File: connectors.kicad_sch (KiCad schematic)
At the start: 67 parts

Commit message: Cosmetic changes
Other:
- moved on the sheet: C?, D?, FB?, J?, Q?, R?, S?, TP?, U?

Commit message: Updated schematic
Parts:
- added J?: JST_XH_1x2_S2B-XH-A-LF-SN, antmicro-footprints:Conn_JST_XH_1x2_S2B-XH-A-LF-SN, symbol antmicroWire2BoardConnectors:JST_XH_1x2_S2B-XH-A-LF-SN
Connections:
- net GND: now also J?.1
- net PSU_ON: now also J?.2
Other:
- note added: "front panel switch connector"
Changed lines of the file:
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@@
   (junction (at 140.97 201.93) (diameter 0) (color 0 0 0 0)
   )
+  (junction (at 190.5 74.295) (diameter 0) (color 0 0 0 0)
+  )
   (junction (at 181.61 210.185) (diameter 0) (color 0 0 0 0)
   )
@@
   (junction (at 140.97 209.55) (diameter 0) (color 0 0 0 0)
   )
+  (junction (at 205.74 77.47) (diameter 0) (color 0 0 0 0)
+  )
   (no_connect (at 203.2 60.325))
   (no_connect (at 116.84 49.53))
@@
     (stroke (width 0) (type default) (color 0 0 0 0))
   )
+  (wire (pts (xy 195.58 83.185) (xy 190.5 83.185))
+    (stroke (width 0) (type default) (color 0 0 0 0))
+  )
   (wire (pts (xy 325.755 85.09) (xy 328.295 85.09))
     (stroke (width 0) (type default) (color 0 0 0 0))
@@
     (stroke (width 0) (type default) (color 0 0 0 0))
   )
+  (wire (pts (xy 198.12 83.185) (xy 198.12 77.47))
+    (stroke (width 0) (type default) (color 0 0 0 0))
+  )
   (wire (pts (xy 64.135 184.15) (xy 65.405 184.15))
     (stroke (width 0) (type default) (color 0 0 0 0))
@@
     (stroke (width 0) (type default) (color 0 0 0 0))
   )
+  (wire (pts (xy 190.5 74.295) (xy 190.5 83.185))
+    (stroke (width 0) (type default) (color 0 0 0 0))
+  )
   (wire (pts (xy 80.01 64.77) (xy 82.55 64.77))
     (stroke (width 0) (type default) (color 0 0 0 0))
@@
     (stroke (width 0) (type default) (color 0 0 0 0))
   )
+  (wire (pts (xy 205.74 77.47) (xy 205.74 78.105))
+    (stroke (width 0) (type default) (color 0 0 0 0))
+  )
   (wire (pts (xy 104.14 156.845) (xy 104.14 159.385))
     (stroke (width 0) (type default) (color 0 0 0 0))
@@
     (stroke (width 0) (type default) (color 0 0 0 0))
   )
+  (wire (pts (xy 198.12 77.47) (xy 205.74 77.47))
+    (stroke (width 0) (type default) (color 0 0 0 0))
+  )
   (wire (pts (xy 104.14 203.2) (xy 104.14 205.74))
     (stroke (width 0) (type default) (color 0 0 0 0))
@@
     (stroke (width 0) (type default) (color 0 0 0 0))
   )
-  (wire (pts (xy 205.74 74.295) (xy 205.74 78.105))
+  (wire (pts (xy 205.74 74.295) (xy 205.74 77.47))
     (stroke (width 0) (type default) (color 0 0 0 0))
   )
@@
     (effects (font (size 2.9972 2.9972)) (justify left bottom))
   )
+  (text "front panel switch connector" (at 186.055 92.075 0)
+    (effects (font (size 1.27 1.27)) (justify left bottom))
+  )
   (text "Power Indicators" (at 327.66 179.705 0)
     (effects (font (size 2.9972 2.9972)) (justify left bottom))
@@
     )
     (pin "1")
+    (pin "2")
+  )
+  (symbol (lib_id "antmicroWire2BoardConnectors:JST_XH_1x2_S2B-XH-A-LF-SN") (at 198.12 83.185 270) (unit 1)
+    (in_bom yes) (on_board yes) (fields_autoplaced)
+    (property "Reference" "J?" (id 0) (at 200.152 86.1644 90)
+      (effects (font (size 1.27 1.27) (thickness 0.15)) (justify left))
+    )
+    (property "Value" "JST_XH_1x2_S2B-XH-A-LF-SN" (id 1) (at 187.96 108.585 0)
+      (effects (font (size 1.27 1.27) (thickness 0.15)) (justify left bottom) hide)
+    )
+    (property "Footprint" "antmicro-footprints:Conn_JST_XH_1x2_S2B-XH-A-LF-SN" (id 2) (at 185.42 108.585 0)
+      (effects (font (size 1.27 1.27) (thickness 0.15)) (justify left bottom) hide)
+    )
+    (property "Datasheet" "https://www.tme.eu/Document/0a99312bb6c67d3f0f7869fe9a023cea/XH.pdf" (id 3) (at 182.88 108.585 0)
+      (effects (font (size 1.27 1.27) (thickness 0.15)) (justify left bottom) hide)
+    )
+    (property "MPN" "S2B-XH-A(LF)(SN)" (id 4) (at 200.152 88.6881 90)
+      (effects (font (size 1.27 1.27) (thickness 0.15)) (justify left))
+    )
+    (property "Manufacturer" "JST Automotive Connectors" (id 5) (at 190.5 108.585 0)
+      (effects (font (size 1.27 1.27) (thickness 0.15)) (justify left bottom) hide)
+    )
+    (property "Author" "Antmicro" (id 6) (at 180.34 108.585 0)
+      (effects (font (size 1.27 1.27) (thickness 0.15)) (justify left bottom) hide)
+    )
+    (property "License" "Apache-2.0" (id 7) (at 177.8 108.585 0)
+      (effects (font (size 1.27 1.27) (thickness 0.15)) (justify left bottom) hide)
+    )
+    (pin "1")

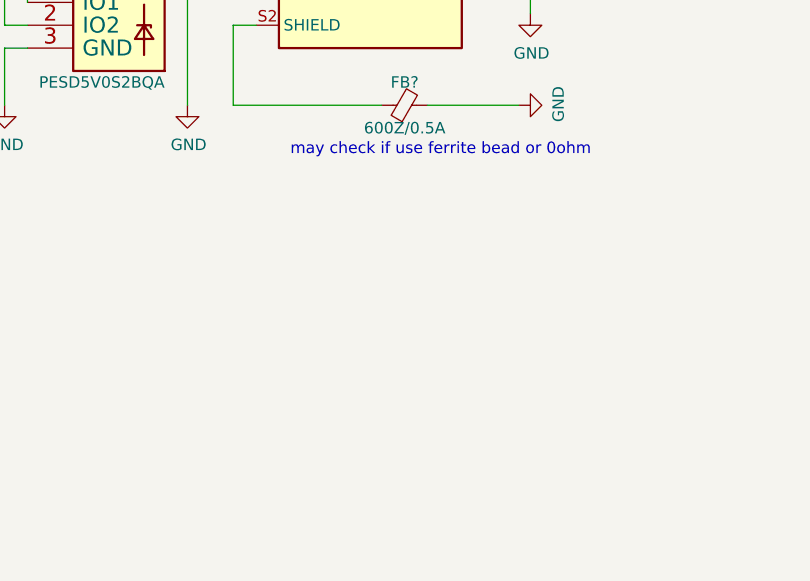
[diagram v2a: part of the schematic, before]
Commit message: Added environmental sensor to the schematic
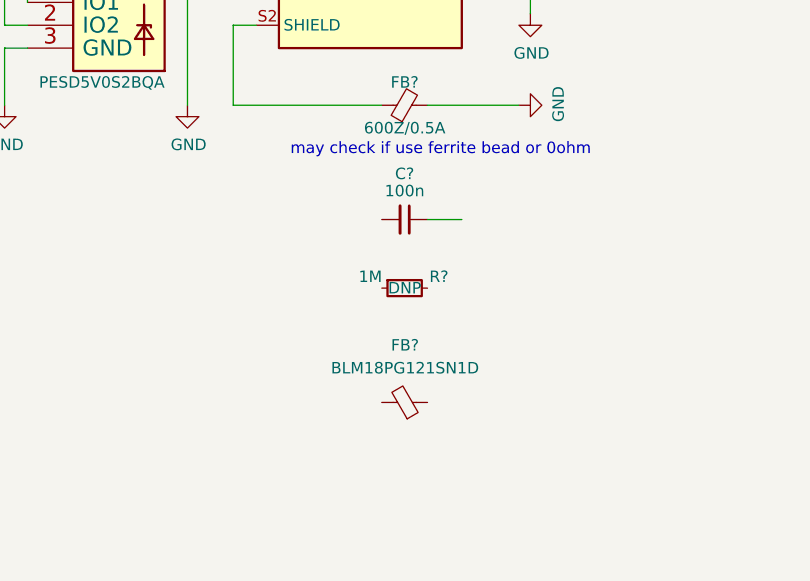
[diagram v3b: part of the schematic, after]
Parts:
- added C?: C_100n_0402, nuc-compute-cluster-environment-sensor-footprints:C_0402_1005Metric, symbol nuc-compute-cluster-environment-sensor:C_100n_0402
- added FB?: FB_120Z_2A_0603, nuc-compute-cluster-environment-sensor-footprints:FB_0603_1608Metric, symbol nuc-compute-cluster-environment-sensor:FB_120Z_2A_0603
- added R?: R_1M_0402, nuc-compute-cluster-environment-sensor-footprints:R_0402_1005Metric, symbol nuc-compute-cluster-environment-sensor:R_1M_0402
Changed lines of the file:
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@@
     (stroke (width 0) (type default) (color 0 0 0 0))
   )
+  (wire (pts (xy 347.345 106.68) (xy 351.155 106.68))
+    (stroke (width 0) (type default) (color 0 0 0 0))
+  )
   (wire (pts (xy 64.135 171.45) (xy 65.405 171.45))
     (stroke (width 0) (type default) (color 0 0 0 0))
@@
     (pin "1")
   )
+  (symbol (lib_id "nuc-compute-cluster-environment-sensor:C_100n_0402") (at 347.345 106.68 180) (unit 1)
+    (in_bom yes) (on_board yes)
+    (property "Reference" "C?" (id 0) (at 344.805 101.6 0)
+      (effects (font (size 1.27 1.27) (thickness 0.15)))
+    )
+    (property "Value" "C_100n_0402" (id 1) (at 327.025 96.52 0)
+      (effects (font (size 1.27 1.27) (thickness 0.15)) (justify left bottom) hide)
+    )
+    (property "Footprint" "nuc-compute-cluster-environment-sensor-footprints:C_0402_1005Metric" (id 2) (at 327.025 93.98 0)
+      (effects (font (size 1.27 1.27) (thickness 0.15)) (justify left bottom) hide)
+    )
+    (property "Datasheet" "https://search.murata.co.jp/Ceramy/image/img/A01X/G101/ENG/GRM155R61H104KE14-01.pdf" (id 3) (at 327.025 91.44 0)
+      (effects (font (size 1.27 1.27) (thickness 0.15)) (justify left bottom) hide)
+    )
+    (property "Manufacturer" "Murata" (id 4) (at 327.025 86.36 0)
+      (effects (font (size 1.27 1.27) (thickness 0.15)) (justify left bottom) hide)
+    )
+    (property "MPN" "GRM155R61H104KE14D" (id 5) (at 327.025 88.9 0)
+      (effects (font (size 1.27 1.27) (thickness 0.15)) (justify left bottom) hide)
+    )
+    (property "Val" "100n" (id 6) (at 344.805 103.505 0)
+      (effects (font (size 1.27 1.27) (thickness 0.15)))
+    )
+    (property "License" "Apache-2.0" (id 7) (at 327.025 83.82 0)
+      (effects (font (size 1.27 1.27) (thickness 0.15)) (justify left bottom) hide)
+    )
+    (property "Author" "Antmicro" (id 8) (at 327.025 81.28 0)
+      (effects (font (size 1.27 1.27) (thickness 0.15)) (justify left bottom) hide)
+    )
+    (property "Voltage" "50V" (id 9) (at 327.025 78.74 0)
+      (effects (font (size 1.27 1.27)) (justify left bottom) hide)
+    )
+    (property "Dielectric" "X5R" (id 10) (at 327.025 76.2 0)
+      (effects (font (size 1.27 1.27)) (justify left bottom) hide)
+    )
+    (pin "1")
+    (pin "2")
+  )
   (symbol (lib_id "antmicroTestPoints:TP_1mm_SMD") (at 80.01 67.31 180) (unit 1)
     (in_bom yes) (on_board yes)
@@
     (pin "1")
   )
+  (symbol (lib_id "nuc-compute-cluster-environment-sensor:R_1M_0402") (at 342.265 114.3 0) (unit 1)
+    (in_bom yes) (on_board yes)
+    (property "Reference" "R?" (id 0) (at 348.615 113.03 0)
+      (effects (font (size 1.27 1.27) (thickness 0.15)))
+    )
+    (property "Value" "R_1M_0402" (id 1) (at 362.585 127 0)
+      (effects (font (size 1.27 1.27) (thickness 0.15)) (justify left bottom) hide)
+    )
+    (property "Footprint" "nuc-compute-cluster-environment-sensor-footprints:R_0402_1005Metric" (id 2) (at 362.585 129.54 0)
+      (effects (font (size 1.27 1.27) (thickness 0.15)) (justify left bottom) hide)
+    )
+    (property "Datasheet" "https://www.bourns.com/docs/product-datasheets/cr.pdf" (id 3) (at 362.585 132.08 0)
+      (effects (font (size 1.27 1.27) (thickness 0.15)) (justify left bottom) hide)
+    )
+    (property "Manufacturer" "Bourns" (id 4) (at 362.585 137.16 0)
+      (effects (font (size 1.27 1.27) (thickness 0.15)) (justify left bottom) hide)
+    )
+    (property "MPN" "CR0402-FX-1004GLF" (id 5) (at 362.585 134.62 0)
+      (effects (font (size 1.27 1.27) (thickness 0.15)) (justify left bottom) hide)
+    )
+    (property "Val" "1M" (id 6) (at 340.995 113.03 0)
+      (effects (font (size 1.27 1.27) (thickness 0.15)))
+    )
+    (property "DNP" "DNP" (id 7) (at 344.805 114.3 0))
+    (property "License" "Apache-2.0" (id 8) (at 362.585 139.7 0)
+      (effects (font (size 1.27 1.27) (thickness 0.15)) (justify left bottom) hide)
+    )
+    (property "Author" "Antmicro" (id 9) (at 362.585 142.24 0)
+      (effects (font (size 1.27 1.27) (thickness 0.15)) (justify left bottom) hide)
+    )
+    (property "Tolerance" "1%" (id 10) (at 362.585 124.46 0)
+      (effects (font (size 1.27 1.27)) (justify left bottom) hide)
+    )
+    (pin "1")
+    (pin "2")
+  )
   (symbol (lib_id "antmicroTestPoints:TP_1mm_SMD") (at 80.01 87.63 180) (unit 1)
     (in_bom yes) (on_board yes)
@@
     (pin "1")
   )
+  (symbol (lib_id "nuc-compute-cluster-environment-sensor:FB_120Z_2A_0603") (at 347.345 127 0) (mirror y) (unit 1)
+    (in_bom yes) (on_board yes) (fields_autoplaced)
+    (property "Reference" "FB?" (id 0) (at 344.8431 120.65 0)
+      (effects (font (size 1.27 1.27) (thickness 0.15)))
+    )
+    (property "Value" "FB_120Z_2A_0603" (id 1) (at 332.105 132.08 0)
+      (effects (font (size 1.27 1.27) (thickness 0.15)) (justify left bottom) hide)
+    )
+    (property "Footprint" "nuc-compute-cluster-environment-sensor-footprints:FB_0603_1608Metric" (id 2) (at 332.105 134.62 0)
+      (effects (font (size 1.27 1.27) (thickness 0.15)) (justify left bottom) hide)
+    )
+    (property "Datasheet" "https://www.murata.com/en-us/products/productdata/8796738650142/ENFA0003.pdf" (id 3) (at 332.105 137.16 0)
+      (effects (font (size 1.27 1.27) (thickness 0.15)) (justify left bottom) hide)
+    )
+    (property "MPN" "BLM18PG121SN1D" (id 4) (at 344.8431 123.19 0)
+      (effects (font (size 1.27 1.27) (thickness 0.15)))
+    )
+    (property "Manufacturer" "Murata" (id 5) (at 332.105 142.24 0)
+      (effects (font (size 1.27 1.27) (thickness 0.15)) (justify left bottom) hide)
+    )
+    (property "Author" "Antmicro" (id 6) (at 332.105 144.78 0)
+      (effects (font (size 1.27 1.27) (thickness 0.15)) (justify left bottom) hide)
+    )
+    (property "License" "Apache-2.0" (id 7) (at 332.105 147.32 0)
+      (effects (font (size 1.27 1.27) (thickness 0.15)) (justify left bottom) hide)
+    )
+    (pin "1")
+    (pin "2")
+  )
   (symbol (lib_id "antmicroFerriteBeadsandChips:FB_600Z_0.5A_Murata-BLM18AG_0603") (at 342.265 93.98 0) (unit 1)

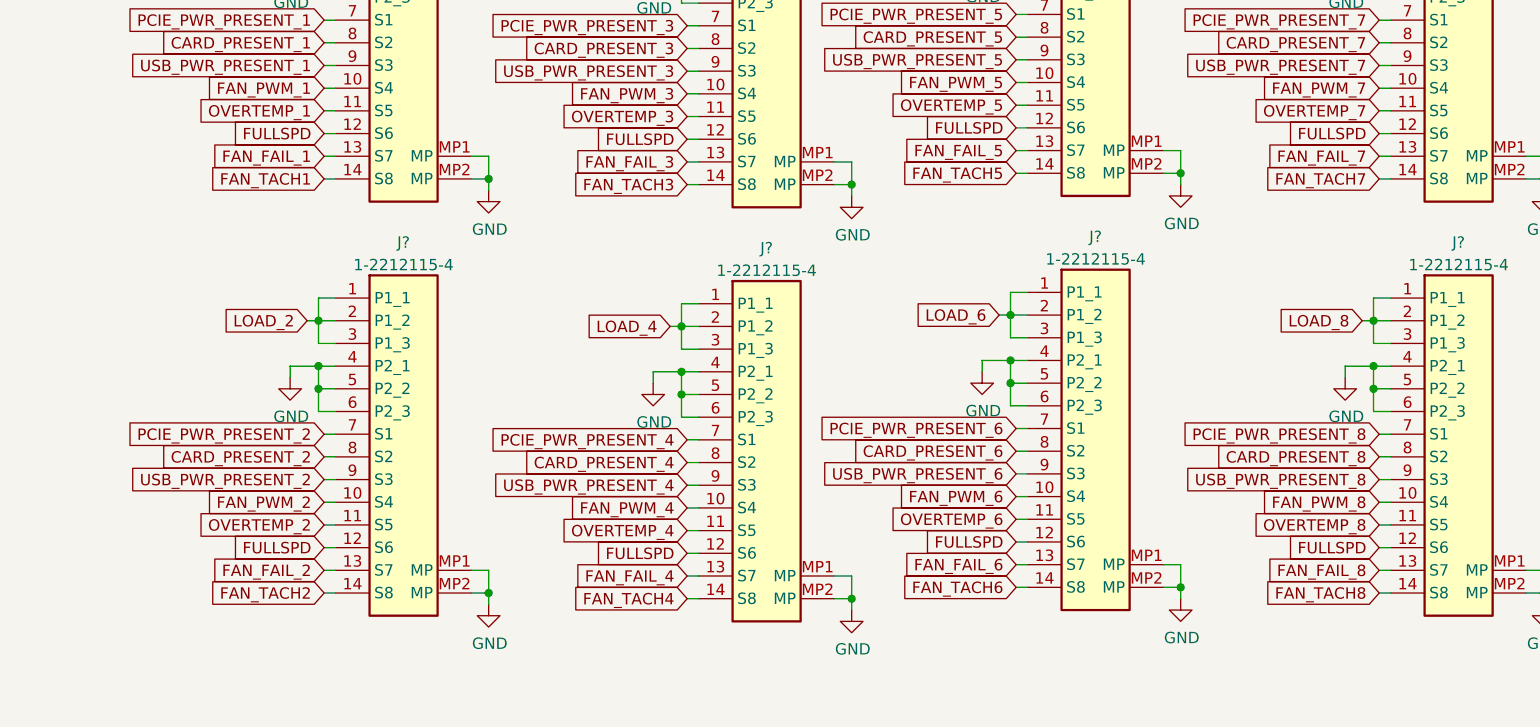
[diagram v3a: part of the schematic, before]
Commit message: Proposed arbiter for controlling fans
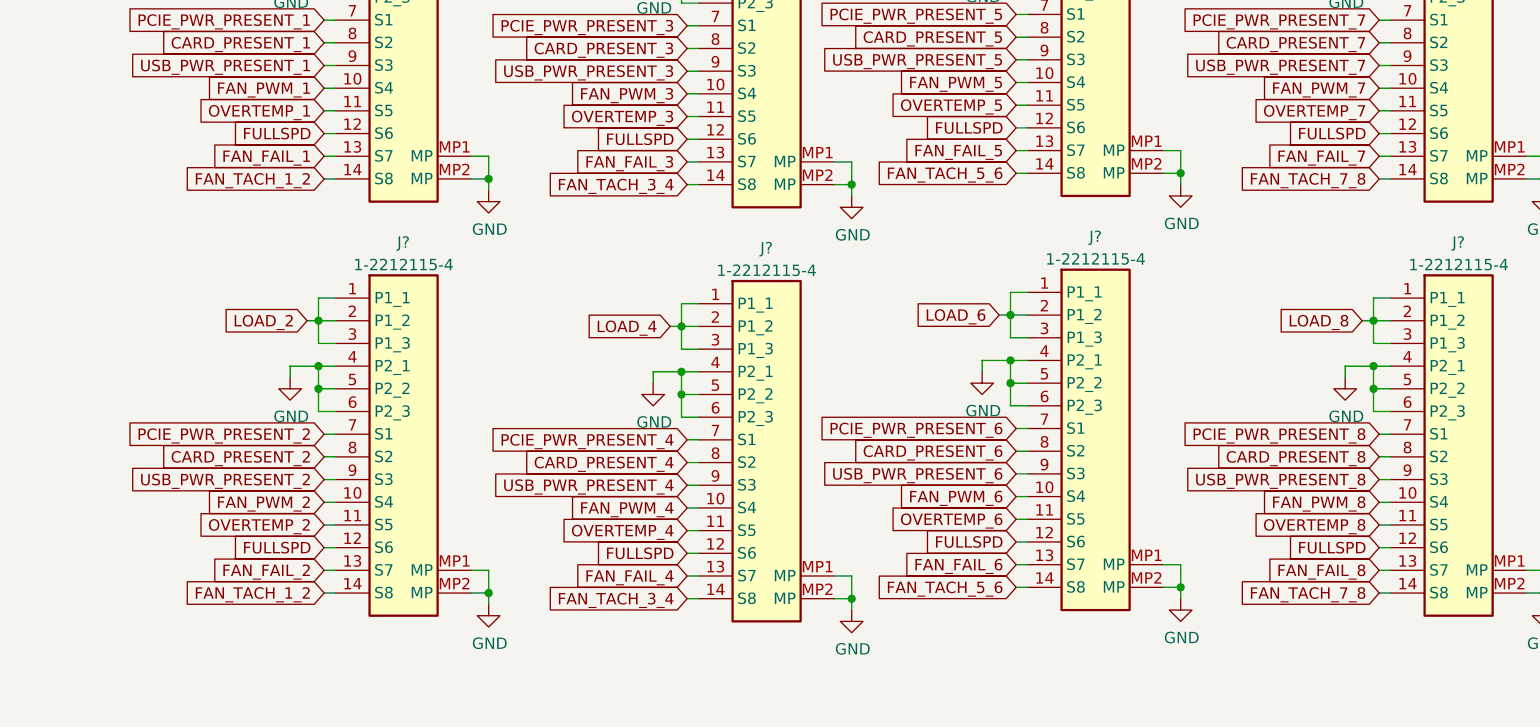
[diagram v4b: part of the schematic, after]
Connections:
- net FAN_TACH2 is gone; now on net FAN_TACH_1_2: J?.14 (S8)
- net FAN_TACH4 is gone; now on net FAN_TACH_3_4: J?.14 (S8)
- net FAN_TACH6 is gone; now on net FAN_TACH_5_6: J?.14 (S8)
- net FAN_TACH8 is gone; now on net FAN_TACH_7_8: J?.14 (S8)
- net FAN_TACH1 renamed FAN_TACH_1_2
- net FAN_TACH3 renamed FAN_TACH_3_4
- net FAN_TACH5 renamed FAN_TACH_5_6
- net FAN_TACH7 renamed FAN_TACH_7_8
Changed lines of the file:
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@@
     )
   )
-  (global_label "FAN_TACH7" (shape input) (at 182.245 186.69 180) (fields_autoplaced)
-    (effects (font (size 1.27 1.27)) (justify right))
-    (property "Intersheet References" "${INTERSHEET_REFS}" (id 0) (at 169.5794 186.6106 0)
+  (global_label "FAN_TACH_7_8" (shape input) (at 182.245 186.69 180) (fields_autoplaced)
+    (effects (font (size 1.27 1.27)) (justify right))
+    (property "Intersheet References" "${INTERSHEET_REFS}" (id 0) (at 166.4346 186.6106 0)
       (effects (font (size 1.27 1.27)) (justify right) hide)
     )
@@
     )
   )
-  (global_label "FAN_TACH5" (shape input) (at 141.605 186.055 180) (fields_autoplaced)
-    (effects (font (size 1.27 1.27)) (justify right))
-    (property "Intersheet References" "${INTERSHEET_REFS}" (id 0) (at 128.9394 185.9756 0)
+  (global_label "FAN_TACH_5_6" (shape input) (at 141.605 186.055 180) (fields_autoplaced)
+    (effects (font (size 1.27 1.27)) (justify right))
+    (property "Intersheet References" "${INTERSHEET_REFS}" (id 0) (at 125.7946 185.9756 0)
       (effects (font (size 1.27 1.27)) (justify right) hide)
     )
@@
     )
   )
-  (global_label "FAN_TACH3" (shape input) (at 104.775 187.325 180) (fields_autoplaced)
-    (effects (font (size 1.27 1.27)) (justify right))
-    (property "Intersheet References" "${INTERSHEET_REFS}" (id 0) (at 92.1094 187.2456 0)
+  (global_label "FAN_TACH_3_4" (shape input) (at 104.775 187.325 180) (fields_autoplaced)
+    (effects (font (size 1.27 1.27)) (justify right))
+    (property "Intersheet References" "${INTERSHEET_REFS}" (id 0) (at 88.9646 187.2456 0)
       (effects (font (size 1.27 1.27)) (justify right) hide)
     )
@@
     )
   )
-  (global_label "FAN_TACH8" (shape input) (at 182.245 233.045 180) (fields_autoplaced)
-    (effects (font (size 1.27 1.27)) (justify right))
-    (property "Intersheet References" "${INTERSHEET_REFS}" (id 0) (at 169.5794 232.9656 0)
+  (global_label "FAN_TACH_7_8" (shape input) (at 182.245 233.045 180) (fields_autoplaced)
+    (effects (font (size 1.27 1.27)) (justify right))
+    (property "Intersheet References" "${INTERSHEET_REFS}" (id 0) (at 166.4346 232.9656 0)
       (effects (font (size 1.27 1.27)) (justify right) hide)
     )
@@
     )
   )
-  (global_label "FAN_TACH2" (shape input) (at 64.135 233.045 180) (fields_autoplaced)
-    (effects (font (size 1.27 1.27)) (justify right))
-    (property "Intersheet References" "${INTERSHEET_REFS}" (id 0) (at 51.4694 232.9656 0)
+  (global_label "FAN_TACH_1_2" (shape input) (at 64.135 233.045 180) (fields_autoplaced)
+    (effects (font (size 1.27 1.27)) (justify right))
+    (property "Intersheet References" "${INTERSHEET_REFS}" (id 0) (at 48.3246 232.9656 0)
       (effects (font (size 1.27 1.27)) (justify right) hide)
     )
@@
     )
   )
-  (global_label "FAN_TACH4" (shape input) (at 104.775 233.68 180) (fields_autoplaced)
-    (effects (font (size 1.27 1.27)) (justify right))
-    (property "Intersheet References" "${INTERSHEET_REFS}" (id 0) (at 92.1094 233.6006 0)
+  (global_label "FAN_TACH_3_4" (shape input) (at 104.775 233.68 180) (fields_autoplaced)
+    (effects (font (size 1.27 1.27)) (justify right))
+    (property "Intersheet References" "${INTERSHEET_REFS}" (id 0) (at 88.9646 233.6006 0)
       (effects (font (size 1.27 1.27)) (justify right) hide)
     )
@@
     )
   )
-  (global_label "FAN_TACH1" (shape input) (at 64.135 186.69 180) (fields_autoplaced)
-    (effects (font (size 1.27 1.27)) (justify right))
-    (property "Intersheet References" "${INTERSHEET_REFS}" (id 0) (at 51.4694 186.6106 0)
+  (global_label "FAN_TACH_1_2" (shape input) (at 64.135 186.69 180) (fields_autoplaced)
+    (effects (font (size 1.27 1.27)) (justify right))
+    (property "Intersheet References" "${INTERSHEET_REFS}" (id 0) (at 48.3246 186.6106 0)
       (effects (font (size 1.27 1.27)) (justify right) hide)
     )
@@
     )
   )
-  (global_label "FAN_TACH6" (shape input) (at 141.605 232.41 180) (fields_autoplaced)
-    (effects (font (size 1.27 1.27)) (justify right))
-    (property "Intersheet References" "${INTERSHEET_REFS}" (id 0) (at 128.9394 232.3306 0)
-      (effects (font (size 1.27 1.27)) (justify right) hide)
-    )
+  (global_label "FAN_TACH_5_6" (shape input) (at 141.605 232.41 180) (fields_autoplaced)
+    (effects (font (size 1.27 1.27)) (justify right))
+    (property "Intersheet References" "${INTERSHEET_REFS}" (id 0) (at 125.7946 232.3306 0)
+      (effects (font (size 1.27 1.27)) (justify right) hide)
+    )
